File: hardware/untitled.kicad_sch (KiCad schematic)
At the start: 22 parts, among them Q1 NMOS, Q2 NMOS, U1 LM51231-Q1

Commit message: making hardware progress
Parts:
- added R56: 1.5mR, symbol Device:R
- renumbered C7 to C1, C8 to C2, C4 to C3, C6 to C4, C2 to C5, C3 to C6, C5 to C7, C1 to C8, Q2 to Q1, Q1 to Q2, R7 to R1, R6 to R2, R5 to R3, R2 to R4, R3 to R5, R20 to R6, R1 to R7, R11 to R8, R4 to R9
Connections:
- net +21V: now also R56.2; no longer C8.2, Q1.1 (D)
- new net 21V_CSN: C8.2, Q1.1 (D), R56.1

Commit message: working on hardware
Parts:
- C1, C2, C5, C6, C7: footprint (none) -> Capacitor_SMD:C_0603_1608Metric
- C3, C4: value 470uF -> 470pF; footprint (none) -> Capacitor_SMD:C_0603_1608Metric
- C8, C9: footprint (none) -> Capacitor_SMD:CP_Elec_10x10.5
- Q1, Q2: footprint (none) -> Package_DFN_QFN:PQFN-8-EP_6x5mm_P1.27mm_Generic
- renumbered R9 to R10, R56 to R9
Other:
- moved on the sheet: C1, C2, C3, C4, C5, C6, C7, C8, C9, L1, Q1, Q2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

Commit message: working assighning footprints still
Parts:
- R1, R2, R3, R4, R5, R7, R8: footprint (none) -> Resistor_SMD:R_0603_1608Metric
- R10, R9: footprint (none) -> Resistor_SMD:R_2512_6332Metric
- R6: footprint (none) -> PCM_Potentiometer_SMD_AKL:Potentiometer_Bourns_TC33X_Vertical
- U1: footprint (none) -> PCM_Package_DFN_QFN_AKL:QFN-20-1EP_3.5x3.5mm_P0.5mm_EP2x2mm_ThermalVias
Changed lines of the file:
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@@
       (effects (font (size 1.27 1.27)))
     )
-    (property "Footprint" "" (at 101.6 137.668 90)
+    (property "Footprint" "PCM_Potentiometer_SMD_AKL:Potentiometer_Bourns_TC33X_Vertical" (at 101.6 137.668 90)
       (effects (font (size 1.27 1.27)) hide)
     )
@@
       (effects (font (size 1.27 1.27)))
     )
-    (property "Footprint" "" (at 82.55 137.668 90)
+    (property "Footprint" "Resistor_SMD:R_0603_1608Metric" (at 82.55 137.668 90)
       (effects (font (size 1.27 1.27)) hide)
     )
@@
       (effects (font (size 1.27 1.27)))
     )
-    (property "Footprint" "" (at 102.87 107.188 90)
+    (property "Footprint" "Resistor_SMD:R_0603_1608Metric" (at 102.87 107.188 90)
       (effects (font (size 1.27 1.27)) hide)
     )
@@
       (effects (font (size 1.27 1.27)) (justify left))
     )
-    (property "Footprint" "" (at 116.332 140.97 90)
+    (property "Footprint" "Resistor_SMD:R_0603_1608Metric" (at 116.332 140.97 90)
       (effects (font (size 1.27 1.27)) hide)
     )
@@
       (effects (font (size 1.27 1.27)))
     )
-    (property "Footprint" "" (at 133.35 83.82 0)
+    (property "Footprint" "PCM_Package_DFN_QFN_AKL:QFN-20-1EP_3.5x3.5mm_P0.5mm_EP2x2mm_ThermalVias" (at 133.35 83.82 0)
       (effects (font (size 1.27 1.27)) hide)
     )
@@
       (effects (font (size 1.27 1.27)) (justify left))
     )
-    (property "Footprint" "" (at 73.152 100.33 90)
+    (property "Footprint" "Resistor_SMD:R_0603_1608Metric" (at 73.152 100.33 90)
       (effects (font (size 1.27 1.27)) hide)
     )
@@
       (effects (font (size 1.27 1.27)))
     )
-    (property "Footprint" "" (at 213.36 109.728 90)
+    (property "Footprint" "Resistor_SMD:R_2512_6332Metric" (at 213.36 109.728 90)
       (effects (font (size 1.27 1.27)) hide)
     )
@@
       (effects (font (size 1.27 1.27)) (justify left))
     )
-    (property "Footprint" "" (at 38.862 110.49 90)
+    (property "Footprint" "Resistor_SMD:R_0603_1608Metric" (at 38.862 110.49 90)
       (effects (font (size 1.27 1.27)) hide)
     )
@@
       (effects (font (size 1.27 1.27)) (justify left))
     )
-    (property "Footprint" "" (at 73.152 86.36 90)
+    (property "Footprint" "Resistor_SMD:R_0603_1608Metric" (at 73.152 86.36 90)
       (effects (font (size 1.27 1.27)) hide)
     )
@@
       (effects (font (size 1.27 1.27)))
     )
-    (property "Footprint" "" (at 92.71 137.668 90)
+    (property "Footprint" "Resistor_SMD:R_0603_1608Metric" (at 92.71 137.668 90)
       (effects (font (size 1.27 1.27)) hide)
     )
@@
       (effects (font (size 1.27 1.27)))
     )
-    (property "Footprint" "" (at 193.04 94.488 90)
-      (effects (font (size 1.27 1.27)) hide)
-    )
+    (property "Footprint" "Resistor_SMD:R_2512_6332Metric" (at 193.04 94.488 90)
+      (effects (font (size 1.27 1.27)) hide)
+    )

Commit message: FINALY starting the pcb
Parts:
- L1: footprint (none) -> CARTHING:IND-6767GZ_VIS
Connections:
- net 21V_CSN: now also Q1.5 (D); no longer Q1.1 (D)
- net GND: now also Q2.1 (S), Q2.2 (S), U1.21 (EP)
- net HI_SW: now also Q1.4 (G); no longer Q1.2 (G)
- net LO_SW: now also Q2.4 (G); no longer Q2.2 (G)
- net SW: now also Q1.1 (S), Q1.2 (S), Q2.5 (D); no longer Q2.1 (D)
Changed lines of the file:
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@@
     )
   )
-  (global_label "MAIN BOOST CLOCK IN" (shape input) (at 118.11 134.62 0) (fields_autoplaced)
-    (effects (font (size 1.27 1.27)) (justify left))
-    (property "Intersheetrefs" "${INTERSHEET_REFS}" (at 142.6059 134.62 0)
-      (effects (font (size 1.27 1.27)) (justify left) hide)
+  (global_label "MAIN BOOST CLOCK IN" (shape input) (at 118.11 128.27 180) (fields_autoplaced)
+    (effects (font (size 1.27 1.27)) (justify right))
+    (property "Intersheetrefs" "${INTERSHEET_REFS}" (at 93.6141 128.27 0)
+      (effects (font (size 1.27 1.27)) (justify right) hide)
     )
   )
@@
     )
   )
-  (symbol (lib_id "Simulation_SPICE:NMOS") (at 181.61 101.6 0) (unit 1)
+  (symbol (lib_id "Device:R_Trim") (at 101.6 135.89 90) (unit 1)
+    (in_bom yes) (on_board yes) (dnp no) (fields_autoplaced)
+    (property "Reference" "R6" (at 101.6 130.4671 90)
+      (effects (font (size 1.27 1.27)))
+    )
+    (property "Value" "1K" (at 101.6 132.3881 90)
+      (effects (font (size 1.27 1.27)))
+    )
+    (property "Footprint" "PCM_Potentiometer_SMD_AKL:Potentiometer_Bourns_TC33X_Vertical" (at 101.6 137.668 90)
+      (effects (font (size 1.27 1.27)) hide)
+    )
+    (property "Datasheet" "~" (at 101.6 135.89 0)
+      (effects (font (size 1.27 1.27)) hide)
+    )
+    (pin "1")
+    (pin "2")
+    (instances
+      (project "usbc-car-module"
+        (path "/fae025e9-99c5-40c1-af6f-99dc1edbfa43/d2e16279-165c-4434-90cd-263b76553257"
+          (reference "R6") (unit 1)
+        )
+      )
+    )
+  )
+  (symbol (lib_id "Device:R") (at 82.55 135.89 90) (unit 1)
+    (in_bom yes) (on_board yes) (dnp no) (fields_autoplaced)
+    (property "Reference" "R4" (at 82.55 131.8641 90)
+      (effects (font (size 1.27 1.27)))
+    )
+    (property "Value" "100K" (at 82.55 133.7851 90)
+      (effects (font (size 1.27 1.27)))
+    )
+    (property "Footprint" "Resistor_SMD:R_0603_1608Metric" (at 82.55 137.668 90)
+      (effects (font (size 1.27 1.27)) hide)
+    )
+    (property "Datasheet" "~" (at 82.55 135.89 0)
+      (effects (font (size 1.27 1.27)) hide)
+    )
+    (pin "1")
+    (pin "2")
+    (instances
+      (project "usbc-car-module"
+        (path "/fae025e9-99c5-40c1-af6f-99dc1edbfa43/d2e16279-165c-4434-90cd-263b76553257"
+          (reference "R4") (unit 1)
+        )
+      )
+    )
+  )
+  (symbol (lib_id "Device:R") (at 102.87 105.41 90) (unit 1)
+    (in_bom yes) (on_board yes) (dnp no) (fields_autoplaced)
+    (property "Reference" "R7" (at 102.87 101.3841 90)
+      (effects (font (size 1.27 1.27)))
+    )
+    (property "Value" "10K" (at 102.87 103.3051 90)
+      (effects (font (size 1.27 1.27)))
+    )
+    (property "Footprint" "Resistor_SMD:R_0603_1608Metric" (at 102.87 107.188 90)
+      (effects (font (size 1.27 1.27)) hide)
+    )
+    (property "Datasheet" "~" (at 102.87 105.41 0)
+      (effects (font (size 1.27 1.27)) hide)
+    )
+    (pin "1")
+    (pin "2")
+    (instances
+      (project "usbc-car-module"
+        (path "/fae025e9-99c5-40c1-af6f-99dc1edbfa43/d2e16279-165c-4434-90cd-263b76553257"
+          (reference "R7") (unit 1)
+        )
+      )
+    )
+  )
+  (symbol (lib_id "power:GND") (at 173.99 90.17 0) (unit 1)
+    (in_bom yes) (on_board yes) (dnp no) (fields_autoplaced)
+    (property "Reference" "#PWR04" (at 173.99 96.52 0)
+      (effects (font (size 1.27 1.27)) hide)
+    )
+    (property "Value" "GND" (at 173.99 94.3055 0)
+      (effects (font (size 1.27 1.27)))
+    )
+    (property "Footprint" "" (at 173.99 90.17 0)
+      (effects (font (size 1.27 1.27)) hide)
+    )
+    (property "Datasheet" "" (at 173.99 90.17 0)
+      (effects (font (size 1.27 1.27)) hide)
+    )
+    (pin "1")
+    (instances
+      (project "usbc-car-module"
+        (path "/fae025e9-99c5-40c1-af6f-99dc1edbfa43/d2e16279-165c-4434-90cd-263b76553257"
+          (reference "#PWR04") (unit 1)
+        )
+      )
+    )
+  )
+  (symbol (lib_name "NMOS_1") (lib_id "Simulation_SPICE:NMOS") (at 181.61 101.6 0) (unit 1)
     (in_bom yes) (on_board yes) (dnp no)
     (property "Reference" "Q1" (at 186.8169 102.2437 0)
@@
     (pin "2")
     (pin "3")
+    (pin "4")
+    (pin "5")
     (instances
       (project "usbc-car-module"
         (path "/fae025e9-99c5-40c1-af6f-99dc1edbfa43/d2e16279-165c-4434-90cd-263b76553257"
           (reference "Q1") (unit 1)
-        )
-      )
-    )
-  )
-  (symbol (lib_id "Device:R_Trim") (at 101.6 135.89 90) (unit 1)
-    (in_bom yes) (on_board yes) (dnp no) (fields_autoplaced)
-    (property "Reference" "R6" (at 101.6 130.4671 90)
-      (effects (font (size 1.27 1.27)))
-    )
-    (property "Value" "1K" (at 101.6 132.3881 90)
-      (effects (font (size 1.27 1.27)))
-    )
-    (property "Footprint" "PCM_Potentiometer_SMD_AKL:Potentiometer_Bourns_TC33X_Vertical" (at 101.6 137.668 90)
-      (effects (font (size 1.27 1.27)) hide)
-    )
-    (property "Datasheet" "~" (at 101.6 135.89 0)
-      (effects (font (size 1.27 1.27)) hide)
-    )
-    (pin "1")
-    (pin "2")
-    (instances
-      (project "usbc-car-module"
-        (path "/fae025e9-99c5-40c1-af6f-99dc1edbfa43/d2e16279-165c-4434-90cd-263b76553257"
-          (reference "R6") (unit 1)
-        )
-      )
-    )
-  )
-  (symbol (lib_id "Device:R") (at 82.55 135.89 90) (unit 1)
-    (in_bom yes) (on_board yes) (dnp no) (fields_autoplaced)
-    (property "Reference" "R4" (at 82.55 131.8641 90)
-      (effects (font (size 1.27 1.27)))
-    )
-    (property "Value" "100K" (at 82.55 133.7851 90)
-      (effects (font (size 1.27 1.27)))
-    )
-    (property "Footprint" "Resistor_SMD:R_0603_1608Metric" (at 82.55 137.668 90)
-      (effects (font (size 1.27 1.27)) hide)
-    )
-    (property "Datasheet" "~" (at 82.55 135.89 0)
-      (effects (font (size 1.27 1.27)) hide)
-    )
-    (pin "1")
-    (pin "2")
-    (instances
-      (project "usbc-car-module"
-        (path "/fae025e9-99c5-40c1-af6f-99dc1edbfa43/d2e16279-165c-4434-90cd-263b76553257"
-          (reference "R4") (unit 1)
-        )
-      )
-    )
-  )
-  (symbol (lib_id "Device:R") (at 102.87 105.41 90) (unit 1)
-    (in_bom yes) (on_board yes) (dnp no) (fields_autoplaced)
-    (property "Reference" "R7" (at 102.87 101.3841 90)
-      (effects (font (size 1.27 1.27)))
-    )
-    (property "Value" "10K" (at 102.87 103.3051 90)
-      (effects (font (size 1.27 1.27)))
-    )
-    (property "Footprint" "Resistor_SMD:R_0603_1608Metric" (at 102.87 107.188 90)
-      (effects (font (size 1.27 1.27)) hide)
-    )
-    (property "Datasheet" "~" (at 102.87 105.41 0)
-      (effects (font (size 1.27 1.27)) hide)
-    )
-    (pin "1")
-    (pin "2")
-    (instances
-      (project "usbc-car-module"
-        (path "/fae025e9-99c5-40c1-af6f-99dc1edbfa43/d2e16279-165c-4434-90cd-263b76553257"
-          (reference "R7") (unit 1)
-        )
-      )
-    )
-  )
-  (symbol (lib_id "power:GND") (at 173.99 90.17 0) (unit 1)
-    (in_bom yes) (on_board yes) (dnp no) (fields_autoplaced)
-    (property "Reference" "#PWR04" (at 173.99 96.52 0)
-      (effects (font (size 1.27 1.27)) hide)
-    )
-    (property "Value" "GND" (at 173.99 94.3055 0)
-      (effects (font (size 1.27 1.27)))
-    )
-    (property "Footprint" "" (at 173.99 90.17 0)
-      (effects (font (size 1.27 1.27)) hide)
-    )
-    (property "Datasheet" "" (at 173.99 90.17 0)
-      (effects (font (size 1.27 1.27)) hide)
-    )
-    (pin "1")
-    (instances
-      (project "usbc-car-module"
-        (path "/fae025e9-99c5-40c1-af6f-99dc1edbfa43/d2e16279-165c-4434-90cd-263b76553257"
-          (reference "#PWR04") (unit 1)
         )
       )
@@
     )
   )
-  (symbol (lib_id "Simulation_SPICE:NMOS") (at 181.61 118.11 0) (unit 1)
+  (symbol (lib_name "NMOS_1") (lib_id "Simulation_SPICE:NMOS") (at 181.61 118.11 0) (unit 1)
     (in_bom yes) (on_board yes) (dnp no)
     (property "Reference" "Q2" (at 186.8169 118.7537 0)
@@
     )
     (pin "1")
-    (pin "2")
     (pin "3")
+    (pin "2")
+    (pin "4")
+    (pin "5")
     (instances
       (project "usbc-car-module"
@@
       (effects (font (size 1.27 1.27)))
     )
-    (property "Footprint" "" (at 198.12 107.95 0)
+    (property "Footprint" "CARTHING:IND-6767GZ_VIS" (at 198.12 107.95 0)
       (effects (font (size 1.27 1.27)) hide)
     )
@@
         )
       )
+    )
+  )
+  (symbol (lib_id "power:GND") (at 142.24 133.35 0) (unit 1)
+    (in_bom yes) (on_board yes) (dnp no) (fields_autoplaced)
+    (property "Reference" "#PWR0148" (at 142.24 139.7 0)
+      (effects (font (size 1.27 1.27)) hide)
+    )
+    (property "Value" "GND" (at 142.24 137.4855 0)
+      (effects (font (size 1.27 1.27)))
+    )
+    (property "Footprint" "" (at 142.24 133.35 0)
+      (effects (font (size 1.27 1.27)) hide)
+    )
+    (property "Datasheet" "" (at 142.24 133.35 0)
+      (effects (font (size 1.27 1.27)) hide)
+    )
+    (pin "1")
+    (instances
+      (project "usbc-car-module"
+        (path "/fae025e9-99c5-40c1-af6f-99dc1edbfa43/d2e16279-165c-4434-90cd-263b76553257"
+          (reference "#PWR0148") (unit 1)
+        )
+      )

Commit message: finaliseing pcb layout will come back later for a fresh look
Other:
- company: (none) -> MICK MAKE
- title: (none) -> 200W USB PD 3.1 HUB
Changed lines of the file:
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@@
 (kicad_sch (version 20230121) (generator eeschema)
   (paper "A4")
+  (title_block
+    (title "200W USB PD 3.1 HUB")
+    (date "2023-10-03")
+    (rev "A")
+    (company "MICK MAKE")
+    (comment 1 "THIS IS A 2X 100W USB PD SOURCE ")
+    (comment 2 "HUB USB SPEC 3.1")
+    (comment 3 "TOTAL SYSTEM POWER IS ~275w")
+  )
   (junction (at 217.17 107.95) (diameter 0) (color 0 0 0 0)
   )

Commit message: messing arround with pcb to finalise
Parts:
- added TP13: TestPoint, TestPoint:TestPoint_Pad_D1.5mm, symbol Connector:TestPoint
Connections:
- net +21V: now also TP13.1
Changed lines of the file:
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@@
   (junction (at 217.17 107.95) (diameter 0) (color 0 0 0 0)
   )
+  (junction (at 199.39 92.71) (diameter 0) (color 0 0 0 0)
+  )
   (junction (at 83.82 113.03) (diameter 0) (color 0 0 0 0)
   )
@@
     (stroke (width 0) (type default))
   )
+  (wire (pts (xy 199.39 92.71) (xy 203.2 92.71))
+    (stroke (width 0) (type default))
+  )
   (wire (pts (xy 154.94 115.57) (xy 157.48 115.57))
     (stroke (width 0) (type default))
@@
     (stroke (width 0) (type default))
   )
-  (wire (pts (xy 196.85 92.71) (xy 203.2 92.71))
+  (wire (pts (xy 196.85 92.71) (xy 199.39 92.71))
     (stroke (width 0) (type default))
   )
@@
         )
       )
+    )
+  )
+  (symbol (lib_id "Connector:TestPoint") (at 199.39 92.71 0) (unit 1)
+    (in_bom yes) (on_board yes) (dnp no) (fields_autoplaced)
+    (property "Reference" "TP13" (at 200.787 88.7643 0)
+      (effects (font (size 1.27 1.27)) (justify left))
+    )
+    (property "Value" "TestPoint" (at 200.787 90.6853 0)
+      (effects (font (size 1.27 1.27)) (justify left))
+    )
+    (property "Footprint" "TestPoint:TestPoint_Pad_D1.5mm" (at 204.47 92.71 0)
+      (effects (font (size 1.27 1.27)) hide)
+    )
+    (property "Datasheet" "~" (at 204.47 92.71 0)
+      (effects (font (size 1.27 1.27)) hide)
+    )
+    (pin "1")
+    (instances
+      (project "usbc-car-module"
+        (path "/fae025e9-99c5-40c1-af6f-99dc1edbfa43/d2e16279-165c-4434-90cd-263b76553257"
+          (reference "TP13") (unit 1)
+        )
+      )

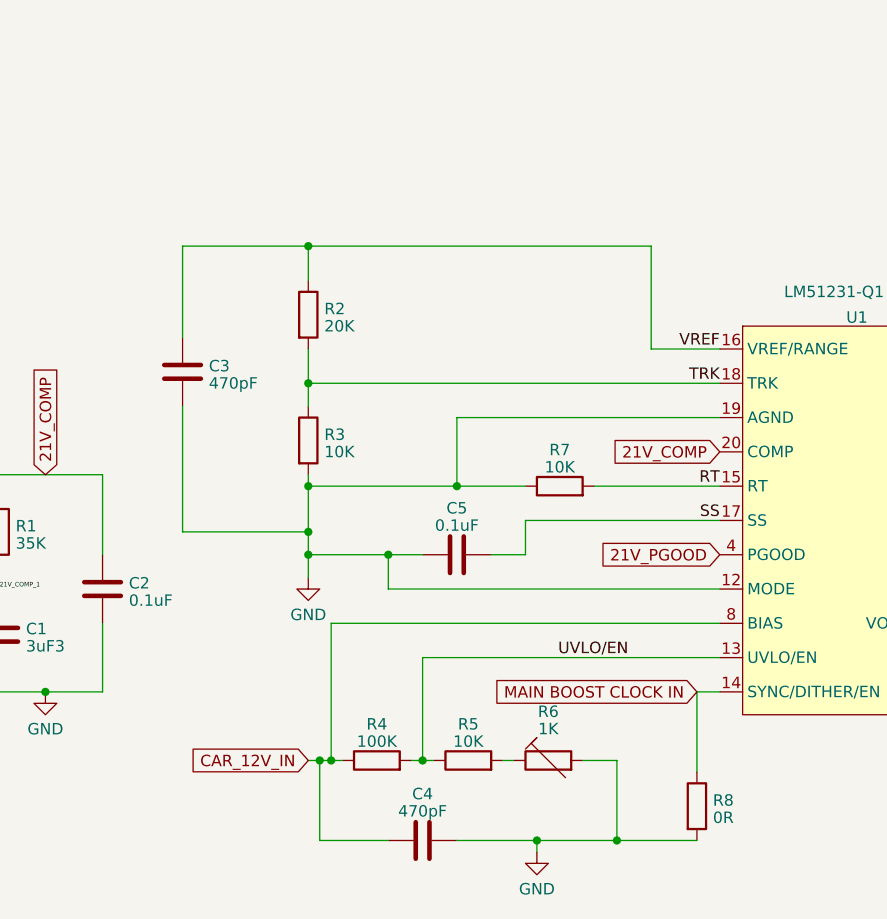
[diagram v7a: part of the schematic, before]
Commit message: fixed DP issues and finneshed overall routeing
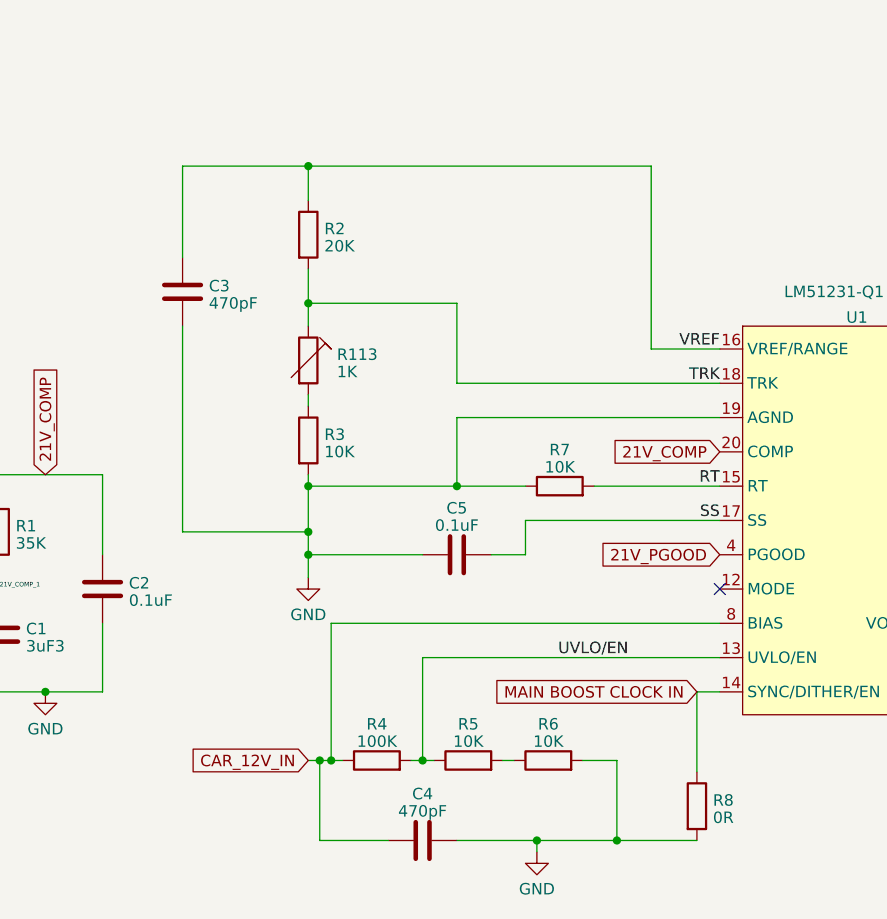
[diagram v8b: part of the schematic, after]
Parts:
- removed R6: 1K, PCM_Potentiometer_SMD_AKL:Potentiometer_Bourns_TC33X_Vertical, symbol Device:R_Trim
- added R113: 1K, Potentiometer_SMD:Potentiometer_Bourns_TC33X_Vertical, symbol Device:R_Trim
- added R6: 10K, Resistor_SMD:R_0603_1608Metric, symbol Device:R
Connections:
- net GND: now also R6.2; no longer U1.12 (MODE)
- net TRK: now also R113.1; no longer R3.1
- net at R5.2: now also R6.1
- new net: R113.2, R3.1
- no-connect marks 0 -> 1
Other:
- moved on the sheet: C3, R2
